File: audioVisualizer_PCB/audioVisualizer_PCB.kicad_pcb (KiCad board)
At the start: 2 copper layers, 65 x 30.5 mm, 26 parts, among them J1 Microphone_Module, J2 USB_B_Micro, J3 SPI_MATRIX, J4 JTAG, U1 STM32F103C8Tx, U2 HT7333, Y1 8Mhz

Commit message: unfinished workflow and update on the TH of the PCB footprint
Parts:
- J3: footprint Connector_PinHeader_1.00mm:PinHeader_1x05_P1.00mm_Vertical -> Connector_PinSocket_2.54mm:PinSocket_1x05_P2.54mm_Vertical
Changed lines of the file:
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@@
 		)
 	)
-	(footprint "Connector_PinHeader_1.00mm:PinHeader_1x05_P1.00mm_Vertical"
+	(footprint "Connector_PinSocket_2.54mm:PinSocket_1x05_P2.54mm_Vertical"
 		(layer "B.Cu")
 		(at 172 59)
-		(descr "Through hole straight pin header, 1x05, 1.00mm pitch, single row")
-		(tags "Through hole pin header THT 1x05 1.00mm single row")
+		(descr "Through hole straight socket strip, 1x05, 2.54mm pitch, single row (from Kicad 4.0.7), script generated")
+		(tags "Through hole socket strip THT 1x05 2.54mm single row")
 		(property "Reference" "J3"
-			(at 0 1.56 0)
+			(at 0 2.77 180)
 			(layer "B.SilkS")
 			(effects
@@
 		)
 		(property "Value" "SPI_MATRIX"
-			(at 0 -5.56 0)
+			(at 0 -12.93 180)
 			(layer "B.Fab")
 			(effects
@@
 		(attr through_hole)
 		(fp_line
-			(start -0.695 -4.56)
-			(end -0.394493 -4.56)
-			(stroke
-				(width 0.12)
-				(type solid)
-			)
-			(layer "B.SilkS")
-		)
-		(fp_line
-			(start -0.695 -0.685)
-			(end -0.695 -4.56)
-			(stroke
-				(width 0.12)
-				(type solid)
-			)
-			(layer "B.SilkS")
-		)
-		(fp_line
-			(start -0.695 -0.685)
-			(end -0.608276 -0.685)
-			(stroke
-				(width 0.12)
-				(type solid)
-			)
-			(layer "B.SilkS")
-		)
-		(fp_line
-			(start -0.695 0)
-			(end -0.695 0.685)
-			(stroke
-				(width 0.12)
-				(type solid)
-			)
-			(layer "B.SilkS")
-		)
-		(fp_line
-			(start -0.695 0.685)
-			(end 0 0.685)
-			(stroke
-				(width 0.12)
-				(type solid)
-			)
-			(layer "B.SilkS")
-		)
-		(fp_line
-			(start 0.394493 -4.56)
-			(end 0.695 -4.56)
-			(stroke
-				(width 0.12)
-				(type solid)
-			)
-			(layer "B.SilkS")
-		)
-		(fp_line
-			(start 0.608276 -0.685)
-			(end 0.695 -0.685)
-			(stroke
-				(width 0.12)
-				(type solid)
-			)
-			(layer "B.SilkS")
-		)
-		(fp_line
-			(start 0.695 -0.685)
-			(end 0.695 -4.56)
-			(stroke
-				(width 0.12)
-				(type solid)
-			)
-			(layer "B.SilkS")
-		)
-		(fp_line
-			(start -1.15 -5)
-			(end 1.15 -5)
-			(stroke
-				(width 0.05)
-				(type solid)
-			)
-			(layer "B.CrtYd")
-		)
-		(fp_line
-			(start -1.15 1)
-			(end -1.15 -5)
-			(stroke
-				(width 0.05)
-				(type solid)
-			)
-			(layer "B.CrtYd")
-		)
-		(fp_line
-			(start 1.15 -5)
-			(end 1.15 1)
-			(stroke
-				(width 0.05)
-				(type solid)
-			)
-			(layer "B.CrtYd")
-		)
-		(fp_line
-			(start 1.15 1)
-			(end -1.15 1)
-			(stroke
-				(width 0.05)
-				(type solid)
-			)
-			(layer "B.CrtYd")
-		)
-		(fp_line
-			(start -0.635 -4.5)
-			(end -0.635 0.1825)
-			(stroke
-				(width 0.1)
-				(type solid)
-			)
-			(layer "B.Fab")
-		)
-		(fp_line
-			(start -0.635 0.1825)
-			(end -0.3175 0.5)
-			(stroke
-				(width 0.1)
-				(type solid)
-			)
-			(layer "B.Fab")
-		)
-		(fp_line
-			(start -0.3175 0.5)
-			(end 0.635 0.5)
-			(stroke
-				(width 0.1)
-				(type solid)
-			)
-			(layer "B.Fab")
-		)
-		(fp_line
-			(start 0.635 -4.5)
-			(end -0.635 -4.5)
-			(stroke
-				(width 0.1)
-				(type solid)
-			)
-			(layer "B.Fab")
-		)
-		(fp_line
-			(start 0.635 0.5)
-			(end 0.635 -4.5)
+			(start -1.33 -11.49)
+			(end 1.33 -11.49)
+			(stroke
+				(width 0.12)
+				(type solid)
+			)
+			(layer "B.SilkS")
+		)
+		(fp_line
+			(start -1.33 -1.27)
+			(end -1.33 -11.49)
+			(stroke
+				(width 0.12)
+				(type solid)
+			)
+			(layer "B.SilkS")
+		)
+		(fp_line
+			(start -1.33 -1.27)
+			(end 1.33 -1.27)
+			(stroke
+				(width 0.12)
+				(type solid)
+			)
+			(layer "B.SilkS")
+		)
+		(fp_line
+			(start 0 1.33)
+			(end 1.33 1.33)
+			(stroke
+				(width 0.12)
+				(type solid)
+			)
+			(layer "B.SilkS")
+		)
+		(fp_line
+			(start 1.33 -1.27)
+			(end 1.33 -11.49)
+			(stroke
+				(width 0.12)
+				(type solid)
+			)
+			(layer "B.SilkS")
+		)
+		(fp_line
+			(start 1.33 1.33)
+			(end 1.33 0)
+			(stroke
+				(width 0.12)
+				(type solid)
+			)
+			(layer "B.SilkS")
+		)
+		(fp_line
+			(start -1.8 -11.9)
+			(end -1.8 1.8)
+			(stroke
+				(width 0.05)
+				(type solid)
+			)
+			(layer "B.CrtYd")
+		)
+		(fp_line
+			(start -1.8 1.8)
+			(end 1.75 1.8)
+			(stroke
+				(width 0.05)
+				(type solid)
+			)
+			(layer "B.CrtYd")
+		)
+		(fp_line
+			(start 1.75 -11.9)
+			(end -1.8 -11.9)
+			(stroke
+				(width 0.05)
+				(type solid)
+			)
+			(layer "B.CrtYd")
+		)
+		(fp_line
+			(start 1.75 1.8)
+			(end 1.75 -11.9)
+			(stroke
+				(width 0.05)
+				(type solid)
+			)
+			(layer "B.CrtYd")
+		)
+		(fp_line
+			(start -1.27 -11.43)
+			(end -1.27 1.27)
+			(stroke
+				(width 0.1)
+				(type solid)
+			)
+			(layer "B.Fab")
+		)
+		(fp_line
+			(start -1.27 1.27)
+			(end 0.635 1.27)
+			(stroke
+				(width 0.1)
+				(type solid)
+			)
+			(layer "B.Fab")
+		)
+		(fp_line
+			(start 0.635 1.27)
+			(end 1.27 0.635)
+			(stroke
+				(width 0.1)
+				(type solid)
+			)
+			(layer "B.Fab")
+		)
+		(fp_line
+			(start 1.27 -11.43)
+			(end -1.27 -11.43)
+			(stroke
+				(width 0.1)
+				(type solid)
+			)
+			(layer "B.Fab")
+		)
+		(fp_line
+			(start 1.27 0.635)
+			(end 1.27 -11.43)
 			(stroke
 				(width 0.1)
@@
 		)
 		(fp_text user "${REFERENCE}"
-			(at 0 -2 90)
-			(layer "B.Fab")
-			(effects
-				(font
-					(size 0.76 0.76)
-					(thickness 0.114)
+			(at 0 -5.08 270)
+			(layer "B.Fab")
+			(effects
+				(font
+					(size 1 1)
+					(thickness 0.15)
 				)
 				(justify mirror)
@@
 		(pad "1" thru_hole rect
 			(at 0 0)
-			(size 0.85 0.85)
-			(drill 0.5)
+			(size 1.7 1.7)
+			(drill 1)
 			(layers "*.Cu" "*.Mask")
 			(remove_unused_layers no)
@@
 		)
 		(pad "2" thru_hole oval
-			(at 0 -1)
-			(size 0.85 0.85)
-			(drill 0.5)
+			(at 0 -2.54)
+			(size 1.7 1.7)
+			(drill 1)
 			(layers "*.Cu" "*.Mask")
 			(remove_unused_layers no)
@@
 		)
 		(pad "3" thru_hole oval
-			(at 0 -2)
-			(size 0.85 0.85)
-			(drill 0.5)
+			(at 0 -5.08)
+			(size 1.7 1.7)
+			(drill 1)
 			(layers "*.Cu" "*.Mask")
 			(remove_unused_layers no)
@@
 		)
 		(pad "4" thru_hole oval
-			(at 0 -3)
-			(size 0.85 0.85)
-			(drill 0.5)
+			(at 0 -7.62)
+			(size 1.7 1.7)
+			(drill 1)
 			(layers "*.Cu" "*.Mask")
 			(remove_unused_layers no)
@@
 		)
 		(pad "5" thru_hole oval
-			(at 0 -4)
-			(size 0.85 0.85)
-			(drill 0.5)
+			(at 0 -10.16)
+			(size 1.7 1.7)
+			(drill 1)
 			(layers "*.Cu" "*.Mask")
 			(remove_unused_layers no)
@@
 		)
 		(embedded_fonts no)
-		(model "${KICAD9_3DMODEL_DIR}/Connector_PinHeader_1.00mm.3dshapes/PinHeader_1x05_P1.00mm_Vertical.wrl"
+		(model "${KICAD9_3DMODEL_DIR}/Connector_PinSocket_2.54mm.3dshapes/PinSocket_1x05_P2.54mm_Vertical.wrl"
 			(offset
 				(xyz 0 0 0)

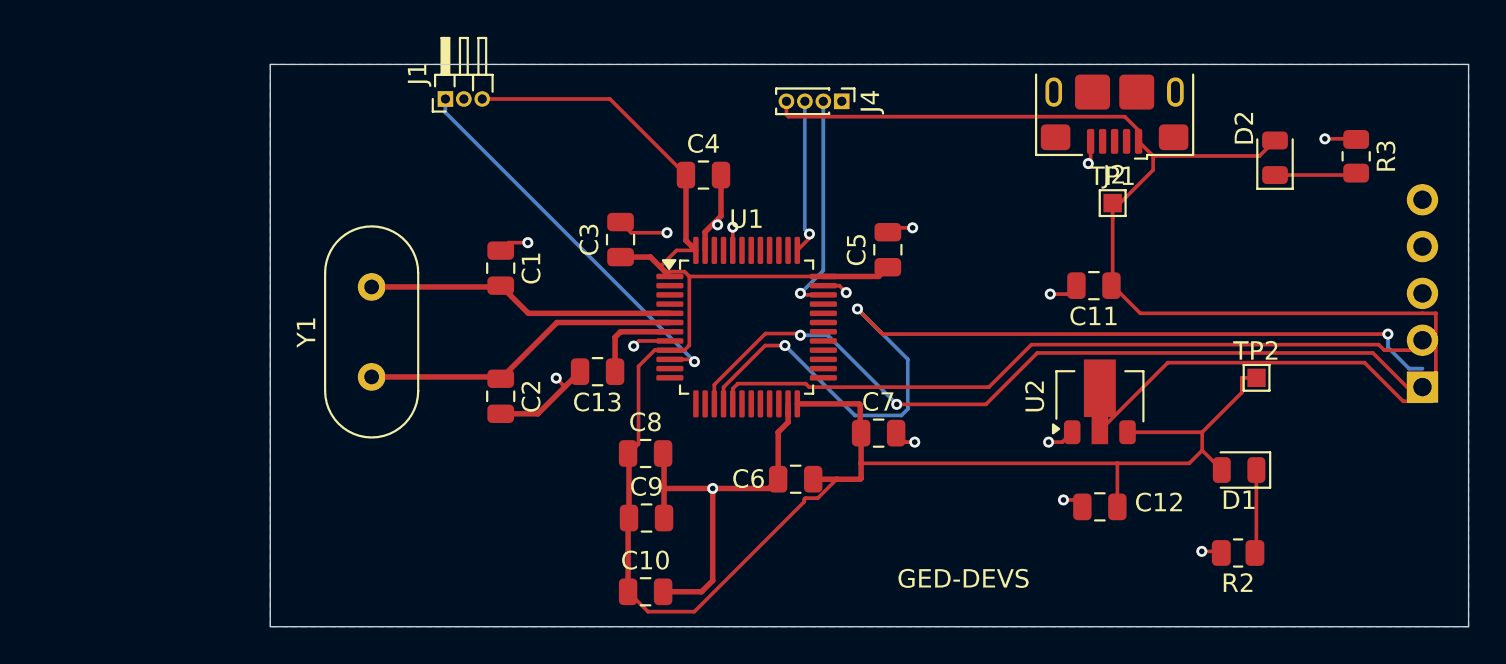
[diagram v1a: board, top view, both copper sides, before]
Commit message: Fixed headerpin diameter, updated workflow
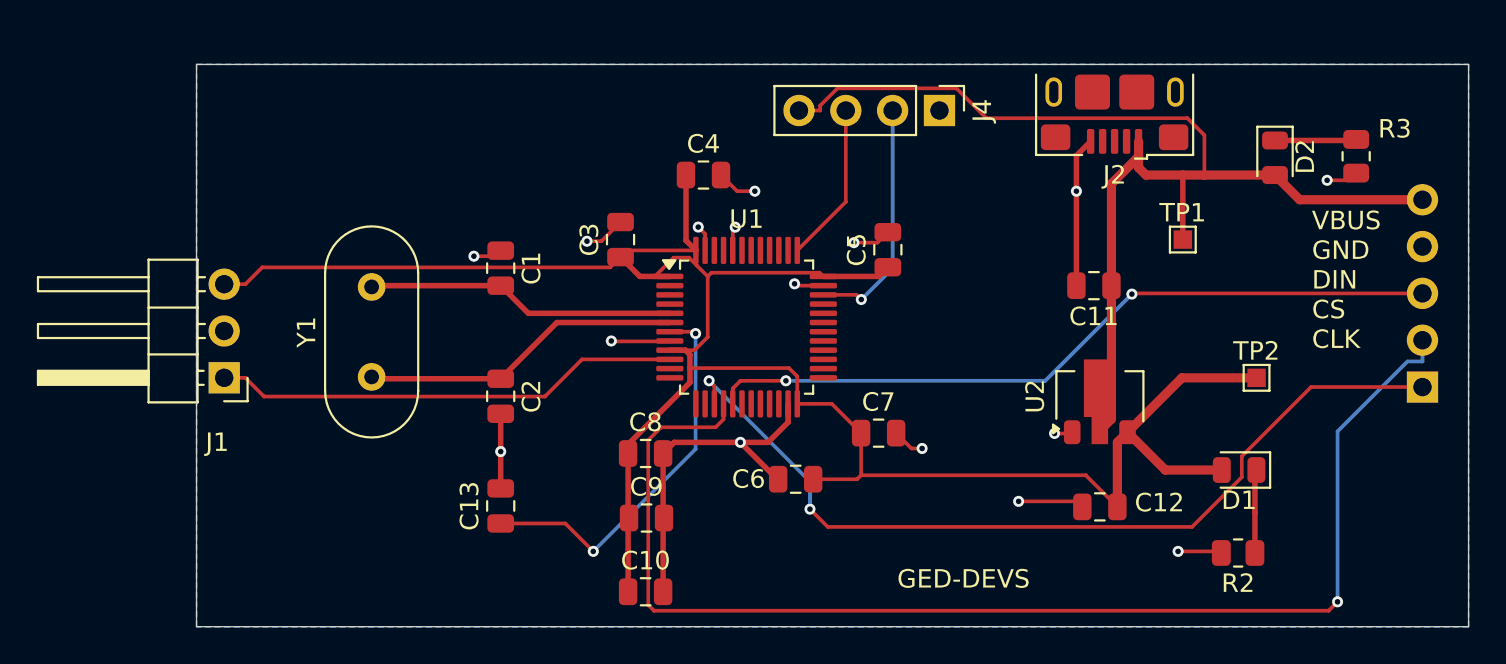
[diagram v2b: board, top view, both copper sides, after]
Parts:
- J1: footprint Connector_PinHeader_1.00mm:PinHeader_1x03_P1.00mm_Horizontal -> Connector_PinHeader_2.54mm:PinHeader_1x03_P2.54mm_Horizontal
- J4: footprint Connector_PinHeader_1.00mm:PinHeader_1x04_P1.00mm_Vertical -> Connector_PinHeader_2.54mm:PinHeader_1x04_P2.54mm_Vertical
- TP2: value TestPoint_3V3 -> TP_3V3
- moved J1 19.3 mm to (107.0, 58.5), turned to 180 degrees
- moved C13 8.98 mm to (122.0, 65.5), turned to 90 degrees
- moved J4 5.32 mm to (145.8, 44.0)
- moved TP1 4.29 mm to (159.0, 51.0)
- turned D2 to -90 degrees
- turned R3 to 90 degrees
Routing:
- net VBUS: track 80.7 -> 62.6 mm
- net Net-(U1-NRST): track 4.96 -> 21.2 mm, vias 0 -> 2
- net /CS: track 52.5 -> 68.6 mm, vias 3 -> 1
- net +3.3V: track 111.9 -> 117.8 mm
- net GND: track 53.4 -> 58.2 mm
- net /OUT: track 21.2 -> 25.4 mm, vias 1 -> 0
- net /CLK: track 44.1 -> 48.0 mm
- net Net-(D1-K): track 4.53 -> 6.74 mm
- net /SWDIO: track 12.2 -> 13.1 mm
- net /DIN: track 39.5 -> 40.4 mm, vias 0 -> 2
- net Net-(J4-Pin_3): track 8.46 -> 8.68 mm, vias 1 -> 0
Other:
- board size 65 x 30.5 mm -> 69 x 30.5 mm
- board text added: "VBUS GND DIN CS CLK"

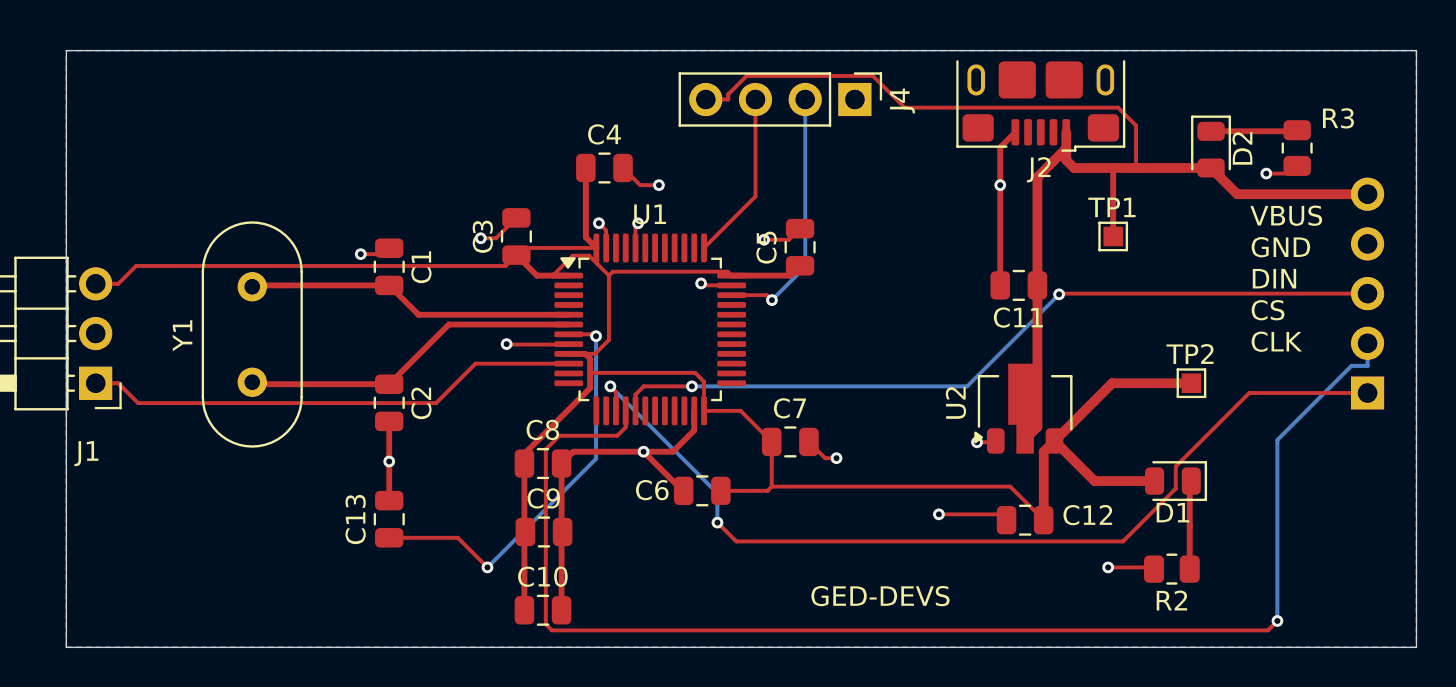
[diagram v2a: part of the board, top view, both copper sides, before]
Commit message: Added additional omni-directional smd mic, not routed or programmed
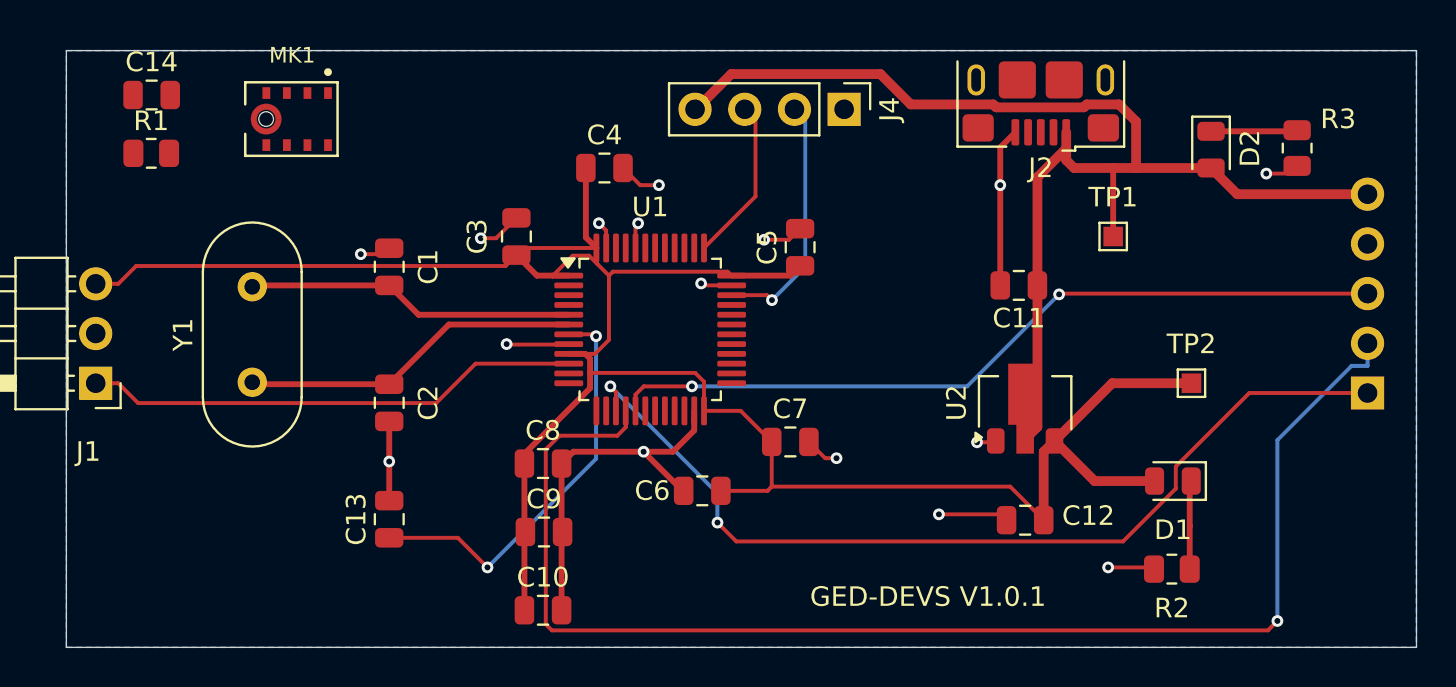
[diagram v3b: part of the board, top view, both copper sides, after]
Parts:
- added C14: C, Capacitor_SMD:C_0805_2012Metric, F.Cu at (109.9, 43.8)
- added MK1: INMP441ACEZ-R7, Microphone:MIC_INMP441ACEZ-R7, F.Cu at (117.0, 45.0)
- added R1: R, Resistor_SMD:R_0805_2012Metric, F.Cu at (109.8, 46.8)
- C11, C12: value 22u -> 10u
- TP2: value TP_3V3 -> TestPoint_3V3
- moved J4 0.74 mm to (145.2, 44.5)
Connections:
- net Net-(J4-Pin_3) renamed /SWCLK
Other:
- board text added: "GED-DEVS V1.0.1"
- board text removed: "GED-DEVS"

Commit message: break em out
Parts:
- added J10: Conn_01x08_Socket, Connector_PinHeader_2.54mm:PinHeader_1x08_P2.54mm_Vertical, F.Cu at (79.9, 35.3)
- added J11: Conn_01x08_Socket, Connector_PinHeader_2.54mm:PinHeader_1x08_P2.54mm_Vertical, F.Cu at (84.5, 35.3)
- added J12: Conn_01x08_Socket, Connector_PinHeader_2.54mm:PinHeader_1x08_P2.54mm_Vertical, F.Cu at (89.1, 35.3)
- added J5: Conn_01x08_Socket, Connector_PinHeader_2.54mm:PinHeader_1x08_P2.54mm_Vertical, F.Cu at (56.9, 35.3)
- added J6: Conn_01x08_Socket, Connector_PinHeader_2.54mm:PinHeader_1x08_P2.54mm_Vertical, F.Cu at (61.5, 35.3)
- added J7: Conn_01x08_Socket, Connector_PinHeader_2.54mm:PinHeader_1x08_P2.54mm_Vertical, F.Cu at (66.1, 35.3)
- added J8: Conn_01x08_Socket, Connector_PinHeader_2.54mm:PinHeader_1x08_P2.54mm_Vertical, F.Cu at (70.7, 35.3)
- added J9: Conn_01x08_Socket, Connector_PinHeader_2.54mm:PinHeader_1x08_P2.54mm_Vertical, F.Cu at (75.3, 35.3)
- added U3: MAX7219, Package_SO:SOIC-24W_7.5x15.4mm_P1.27mm, F.Cu at (110.1, 21.5)
- added U4: MAX7219, Package_SO:SOIC-24W_7.5x15.4mm_P1.27mm, F.Cu at (61.1, 24.5)
- added U5: MAX7219, Package_SO:SOIC-24W_7.5x15.4mm_P1.27mm, F.Cu at (74.0, 24.5)
- added U6: MAX7219, Package_SO:SOIC-24W_7.5x15.4mm_P1.27mm, F.Cu at (86.9, 24.5)
- moved C14 30.9 mm to (94.9, 70.9)
- moved C10 30.9 mm to (114.9, 97.2)
- moved C12 30.9 mm to (139.6, 92.6)
- moved C5 30.9 mm to (128.1, 78.6)
- moved C8 30.9 mm to (114.9, 89.7)
- moved D2 30.9 mm to (149.1, 73.7)
- moved J2 30.9 mm to (140.4, 70.1)
- moved J3 30.9 mm to (157.1, 86.1)
- moved J4 30.9 mm to (130.3, 71.6)
- moved R2 30.9 mm to (147.1, 95.1)
- moved TP1 30.9 mm to (144.1, 78.1)
- moved TP2 30.9 mm to (148.1, 85.6)
- moved U2 30.9 mm to (139.6, 86.6)
- moved C1 30.9 mm to (107.1, 79.6)
- moved C13 30.9 mm to (107.1, 92.5)
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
